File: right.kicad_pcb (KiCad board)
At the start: 2 copper layers, 140 x 27 mm, 11 parts, among them J1 FFC_Connector_13P

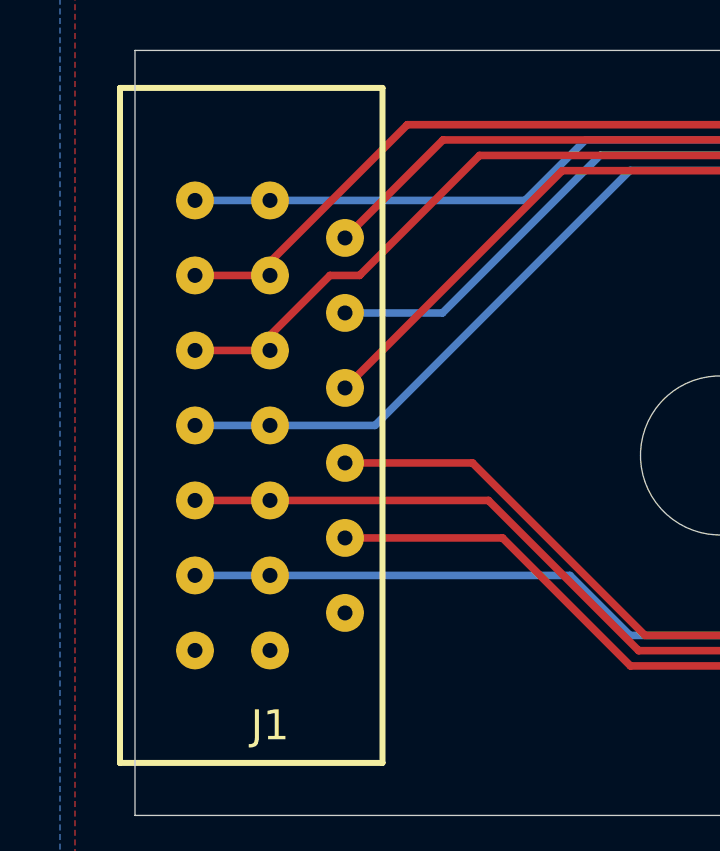
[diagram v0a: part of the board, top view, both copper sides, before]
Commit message: Increase ffc connector hole size to 0.6 mm
The wires on the connector actually measure up to 0.57 mm.
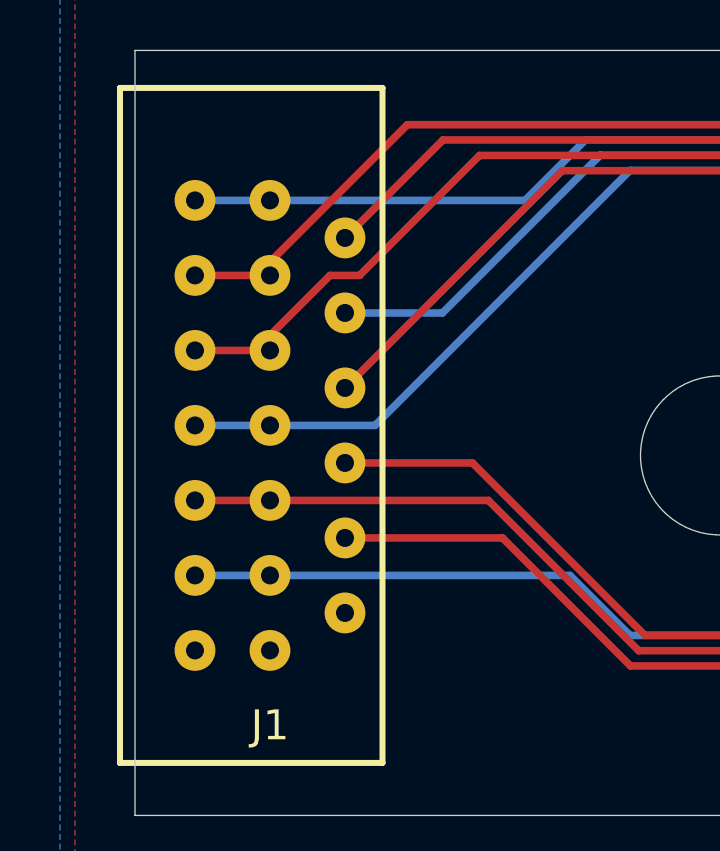
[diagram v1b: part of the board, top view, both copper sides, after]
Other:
- board text added: "V1.2 2022-04-30"
- board text removed: "V1.1 2022-04-22"
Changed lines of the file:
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@@
   (title_block
     (title "Kinesis classic fn row right")
-    (rev v1.1)
+    (rev v1.2)
     (comment 3 "License: MIT")
     (comment 4 "Author: Kyle Stemen")
   )
   (layers
-    (0 F.Cu signal)
-    (31 B.Cu signal)
+    (0 F.Cu signal hide)
+    (31 B.Cu signal hide)
     (32 B.Adhes user)
     (33 F.Adhes user)
@@
       (effects (font (size 1 1) (thickness 0.15)))
     )
+    (fp_line (start -11.25 5) (end 11.25 5) (layer F.Fab) (width 0.15))
+    (fp_line (start -11.25 -3.75) (end 11.25 -3.75) (layer F.Fab) (width 0.15))
+    (fp_line (start 11.25 -3.75) (end 11.25 5) (layer F.Fab) (width 0.15))
+    (fp_line (start -11.25 5) (end -11.25 -3.75) (layer F.Fab) (width 0.15))
+    (fp_line (start -11.25 5) (end -11.25 -3.75) (layer F.SilkS) (width 0.2))
+    (fp_line (start -11.25 -3.75) (end 11.25 -3.75) (layer F.SilkS) (width 0.2))
+    (fp_line (start 11.25 -3.75) (end 11.25 5) (layer F.SilkS) (width 0.2))
     (fp_line (start 11.25 5) (end -11.25 5) (layer F.SilkS) (width 0.2))
-    (fp_line (start 11.25 -3.75) (end 11.25 5) (layer F.SilkS) (width 0.2))
-    (fp_line (start -11.25 -3.75) (end 11.25 -3.75) (layer F.SilkS) (width 0.2))
-    (fp_line (start -11.25 5) (end -11.25 -3.75) (layer F.SilkS) (width 0.2))
-    (fp_line (start -11.25 5) (end -11.25 -3.75) (layer F.Fab) (width 0.15))
-    (fp_line (start 11.25 -3.75) (end 11.25 5) (layer F.Fab) (width 0.15))
-    (fp_line (start -11.25 -3.75) (end 11.25 -3.75) (layer F.Fab) (width 0.15))
-    (fp_line (start -11.25 5) (end 11.25 5) (layer F.Fab) (width 0.15))
-    (pad 13B thru_hole circle (at 7.5 2.5 270) (size 1.262 1.262) (drill 0.5) (layers *.Cu *.Mask)
-      (net 1 GND))
-    (pad 11B thru_hole circle (at 5 2.5 270) (size 1.262 1.262) (drill 0.5) (layers *.Cu *.Mask)
+    (pad 13B thru_hole circle (at 7.5 2.5 270) (size 1.362 1.362) (drill 0.6) (layers *.Cu *.Mask)
+      (net 1 GND))
+    (pad 11B thru_hole circle (at 5 2.5 270) (size 1.362 1.362) (drill 0.6) (layers *.Cu *.Mask)
       (net 7 "Net-(J1-Pad11)"))
-    (pad 9B thru_hole circle (at 2.5 2.5 270) (size 1.262 1.262) (drill 0.5) (layers *.Cu *.Mask)
+    (pad 9B thru_hole circle (at 2.5 2.5 270) (size 1.362 1.362) (drill 0.6) (layers *.Cu *.Mask)
       (net 6 "Net-(F12-Pad2)"))
-    (pad 7B thru_hole circle (at 0 2.5 270) (size 1.262 1.262) (drill 0.5) (layers *.Cu *.Mask)
+    (pad 7B thru_hole circle (at 0 2.5 270) (size 1.362 1.362) (drill 0.6) (layers *.Cu *.Mask)
       (net 5 "Net-(F11-Pad2)"))
-    (pad 5B thru_hole circle (at -2.5 2.5 270) (size 1.262 1.262) (drill 0.5) (layers *.Cu *.Mask)
+    (pad 5B thru_hole circle (at -2.5 2.5 270) (size 1.362 1.362) (drill 0.6) (layers *.Cu *.Mask)
       (net 3 "Net-(F12-Pad4)"))
-    (pad 3B thru_hole circle (at -5 2.5 270) (size 1.262 1.262) (drill 0.5) (layers *.Cu *.Mask)
+    (pad 3B thru_hole circle (at -5 2.5 270) (size 1.362 1.362) (drill 0.6) (layers *.Cu *.Mask)
       (net 12 "Net-(J1-Pad3)"))
-    (pad 1B thru_hole circle (at -7.5 2.5 270) (size 1.262 1.262) (drill 0.5) (layers *.Cu *.Mask)
+    (pad 1B thru_hole circle (at -7.5 2.5 270) (size 1.362 1.362) (drill 0.6) (layers *.Cu *.Mask)
       (net 8 "Net-(J1-Pad1)"))
-    (pad 12 thru_hole circle (at 6.25 -2.5 270) (size 1.262 1.262) (drill 0.5) (layers *.Cu *.Mask))
-    (pad 10 thru_hole circle (at 3.75 -2.5 270) (size 1.262 1.262) (drill 0.5) (layers *.Cu *.Mask)
+    (pad 12 thru_hole circle (at 6.25 -2.5 270) (size 1.362 1.362) (drill 0.6) (layers *.Cu *.Mask))
+    (pad 10 thru_hole circle (at 3.75 -2.5 270) (size 1.362 1.362) (drill 0.6) (layers *.Cu *.Mask)
       (net 9 "Net-(J1-Pad10)"))
-    (pad 8 thru_hole circle (at 1.25 -2.5 270) (size 1.262 1.262) (drill 0.5) (layers *.Cu *.Mask)
+    (pad 8 thru_hole circle (at 1.25 -2.5 270) (size 1.362 1.362) (drill 0.6) (layers *.Cu *.Mask)
       (net 4 "Net-(F10-Pad4)"))
-    (pad 6 thru_hole circle (at -1.25 -2.5 270) (size 1.262 1.262) (drill 0.5) (layers *.Cu *.Mask)
+    (pad 6 thru_hole circle (at -1.25 -2.5 270) (size 1.362 1.362) (drill 0.6) (layers *.Cu *.Mask)
       (net 2 "Net-(F10-Pad2)"))
-    (pad 4 thru_hole circle (at -3.75 -2.5 270) (size 1.262 1.262) (drill 0.5) (layers *.Cu *.Mask)
+    (pad 4 thru_hole circle (at -3.75 -2.5 270) (size 1.362 1.362) (drill 0.6) (layers *.Cu *.Mask)
       (net 10 "Net-(J1-Pad4)"))
-    (pad 2 thru_hole circle (at -6.25 -2.5 270) (size 1.262 1.262) (drill 0.5) (layers *.Cu *.Mask)
+    (pad 2 thru_hole circle (at -6.25 -2.5 270) (size 1.362 1.362) (drill 0.6) (layers *.Cu *.Mask)
       (net 11 "Net-(J1-Pad2)"))
-    (pad 13 thru_hole circle (at 7.5 0 270) (size 1.262 1.262) (drill 0.5) (layers *.Cu *.Mask)
-      (net 1 GND))
-    (pad 11 thru_hole circle (at 5 0 270) (size 1.262 1.262) (drill 0.5) (layers *.Cu *.Mask)
+    (pad 13 thru_hole circle (at 7.5 0 270) (size 1.362 1.362) (drill 0.6) (layers *.Cu *.Mask)
+      (net 1 GND))
+    (pad 11 thru_hole circle (at 5 0 270) (size 1.362 1.362) (drill 0.6) (layers *.Cu *.Mask)
       (net 7 "Net-(J1-Pad11)"))
-    (pad 9 thru_hole circle (at 2.5 0 270) (size 1.262 1.262) (drill 0.5) (layers *.Cu *.Mask)
+    (pad 9 thru_hole circle (at 2.5 0 270) (size 1.362 1.362) (drill 0.6) (layers *.Cu *.Mask)
       (net 6 "Net-(F12-Pad2)"))
-    (pad 7 thru_hole circle (at 0 0 270) (size 1.262 1.262) (drill 0.5) (layers *.Cu *.Mask)
+    (pad 7 thru_hole circle (at 0 0 270) (size 1.362 1.362) (drill 0.6) (layers *.Cu *.Mask)
       (net 5 "Net-(F11-Pad2)"))
-    (pad 5 thru_hole circle (at -2.5 0 270) (size 1.262 1.262) (drill 0.5) (layers *.Cu *.Mask)
+    (pad 5 thru_hole circle (at -2.5 0 270) (size 1.362 1.362) (drill 0.6) (layers *.Cu *.Mask)
       (net 3 "Net-(F12-Pad4)"))
-    (pad 3 thru_hole circle (at -5 0 270) (size 1.262 1.262) (drill 0.5) (layers *.Cu *.Mask)
+    (pad 3 thru_hole circle (at -5 0 270) (size 1.362 1.362) (drill 0.6) (layers *.Cu *.Mask)
       (net 12 "Net-(J1-Pad3)"))
-    (pad 1 thru_hole circle (at -7.5 0 270) (size 1.262 1.262) (drill 0.5) (layers *.Cu *.Mask)
+    (pad 1 thru_hole circle (at -7.5 0 270) (size 1.362 1.362) (drill 0.6) (layers *.Cu *.Mask)
       (net 8 "Net-(J1-Pad1)"))
   )
@@
     (effects (font (size 1.5 1.5) (thickness 0.3)) (justify mirror))
   )
-  (gr_text "V1.1 2022-04-22" (at 187.5 104.5) (layer B.SilkS)
+  (gr_text "V1.2 2022-04-30" (at 187.5 104.5) (layer B.SilkS)
     (effects (font (size 1.5 1.5) (thickness 0.3)) (justify mirror))
   )

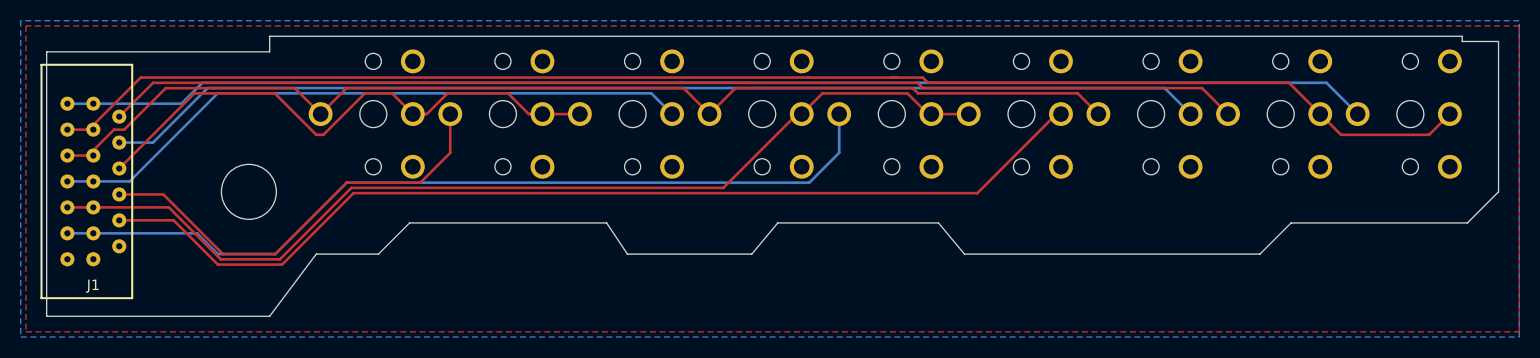
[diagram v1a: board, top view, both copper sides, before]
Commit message: Shift the key switches on the right PCB over 0.6 mm
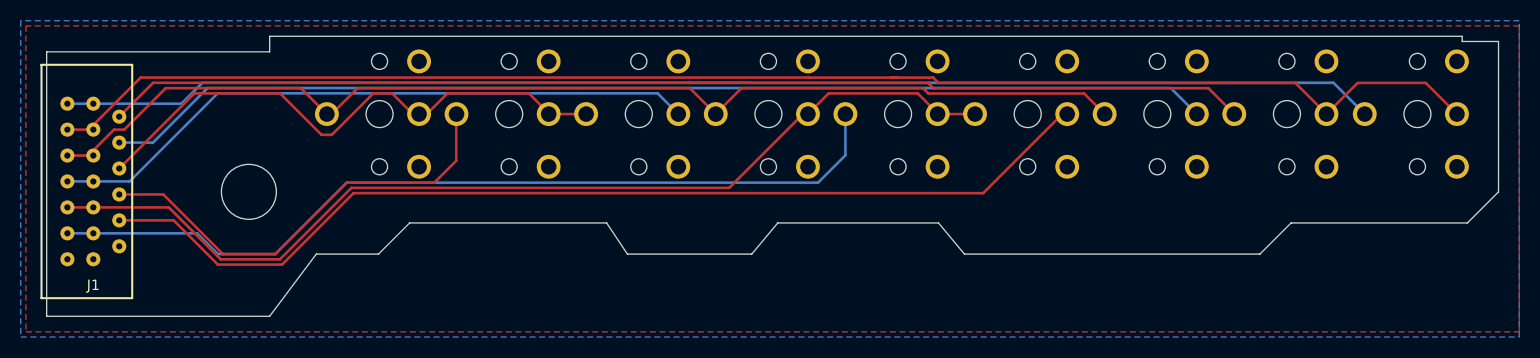
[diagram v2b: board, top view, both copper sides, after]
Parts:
- moved PG1 0.68 mm to (212.2, 96.0)
- moved F10 0.60 mm to (124.6, 96.0)
- moved F11 0.60 mm to (137.1, 96.0)
- moved F12 0.60 mm to (149.6, 96.0)
- moved F9 0.60 mm to (112.1, 96.0)
- moved KP1 0.60 mm to (199.6, 96.0)
- moved P-B1 0.60 mm to (187.1, 96.0)
- moved P-S1 0.60 mm to (162.1, 96.0)
- moved S-L1 0.60 mm to (174.6, 96.0)
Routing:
- net Net-(J1-Pad3): track 139.3 -> 140.8 mm
- net Net-(F10-Pad4): track 42.1 -> 43.1 mm
- net Net-(J1-Pad11): track 83.0 -> 83.8 mm
- net Net-(J1-Pad4): track 106.5 -> 107.1 mm
- net Net-(F11-Pad2): track 62.7 -> 63.3 mm
- net Net-(J1-Pad2): track 109.5 -> 110.1 mm
- net Net-(F12-Pad4): track 107.6 -> 108.2 mm
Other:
- board text added: "V1.3 2022-05-08"
- board text removed: "V1.2 2022-04-30"
